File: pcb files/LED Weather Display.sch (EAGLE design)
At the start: 9 parts, among them IC1 74HCT245N, J1 POWER_JACK

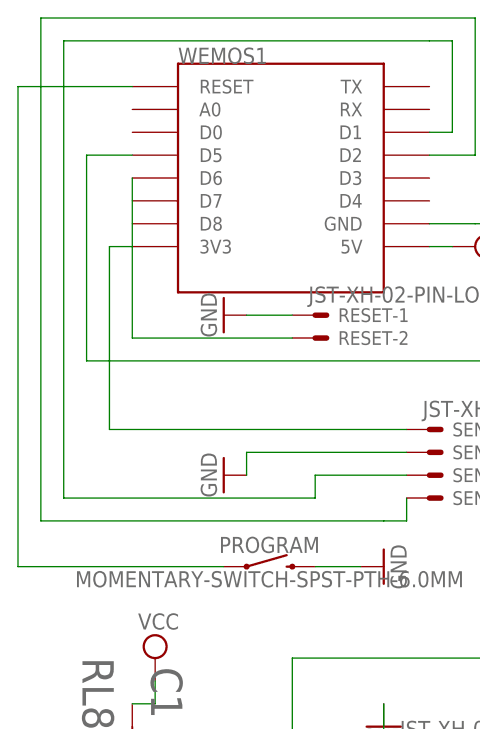
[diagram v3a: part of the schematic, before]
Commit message: PCB traces were incorrect for reset.
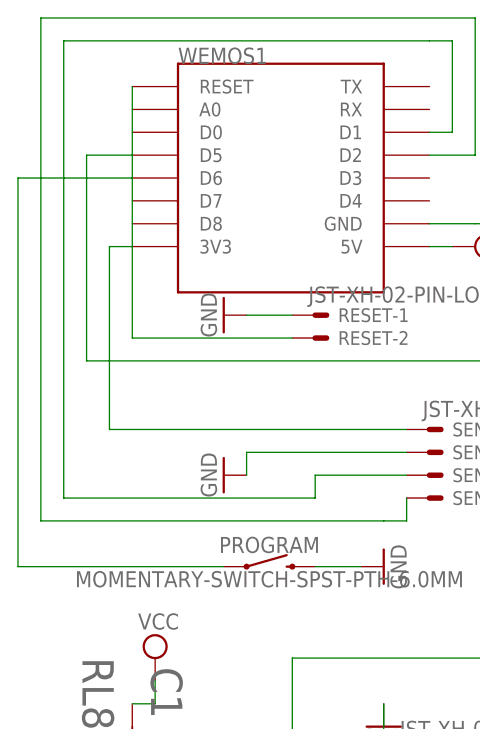
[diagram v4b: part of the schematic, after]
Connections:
- net N$7: now also WEMOS1.D6; no longer WEMOS1.RESET
- net N$8: now also WEMOS1.RESET; no longer WEMOS1.D6
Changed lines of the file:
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@@
 <pinref part="PROGRAM" gate="G$1" pin="1"/>
 <wire x1="10.16" y1="25.4" x2="-12.7" y2="25.4" width="0.1524" layer="91"/>
-<pinref part="WEMOS1" gate="D1" pin="RESET"/>
-<wire x1="-12.7" y1="25.4" x2="-12.7" y2="78.74" width="0.1524" layer="91"/>
-<wire x1="-12.7" y1="78.74" x2="0" y2="78.74" width="0.1524" layer="91"/>
+<pinref part="WEMOS1" gate="D1" pin="D6"/>
+<wire x1="0" y1="68.58" x2="-12.7" y2="68.58" width="0.1524" layer="91"/>
+<wire x1="-12.7" y1="68.58" x2="-12.7" y2="25.4" width="0.1524" layer="91"/>
 </segment>
 </net>
@@
 <pinref part="RESET" gate="-2" pin="S"/>
 <wire x1="17.78" y1="50.8" x2="0" y2="50.8" width="0.1524" layer="91"/>
-<pinref part="WEMOS1" gate="D1" pin="D6"/>
-<wire x1="0" y1="50.8" x2="0" y2="68.58" width="0.1524" layer="91"/>
+<pinref part="WEMOS1" gate="D1" pin="RESET"/>
+<wire x1="0" y1="50.8" x2="0" y2="78.74" width="0.1524" layer="91"/>
 </segment>
 </net>
